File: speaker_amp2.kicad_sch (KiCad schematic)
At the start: 59 parts, among them U1 TAS5822MDCPR, U2 TAS5822MDCPR

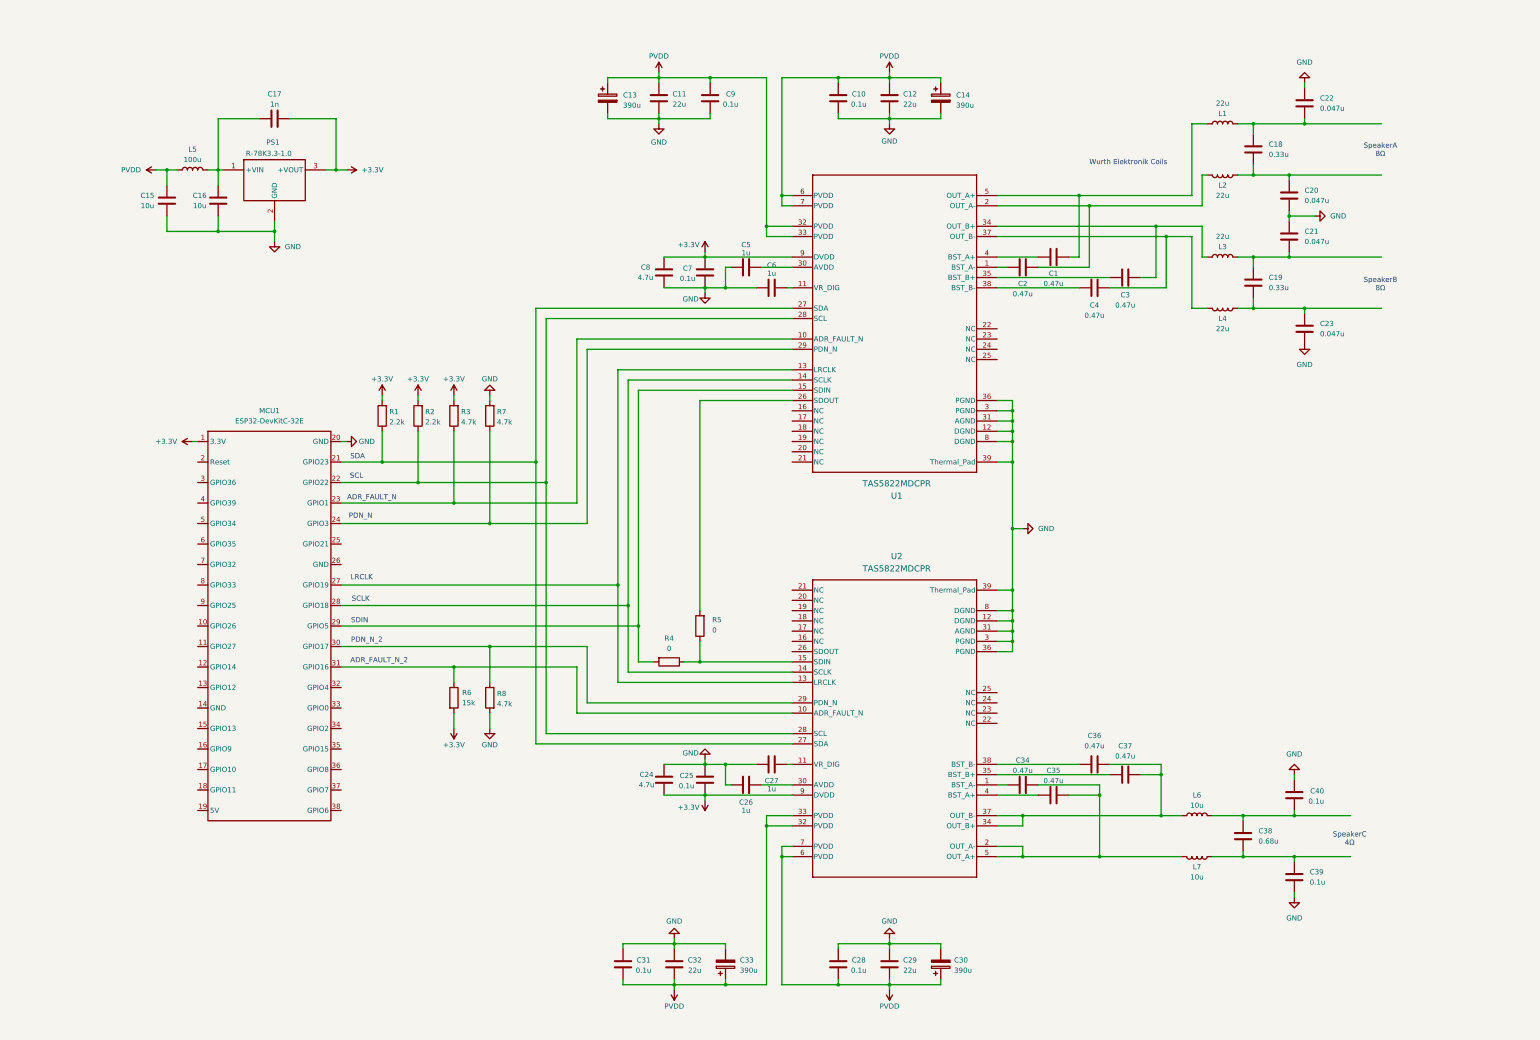
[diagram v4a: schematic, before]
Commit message: added connectors
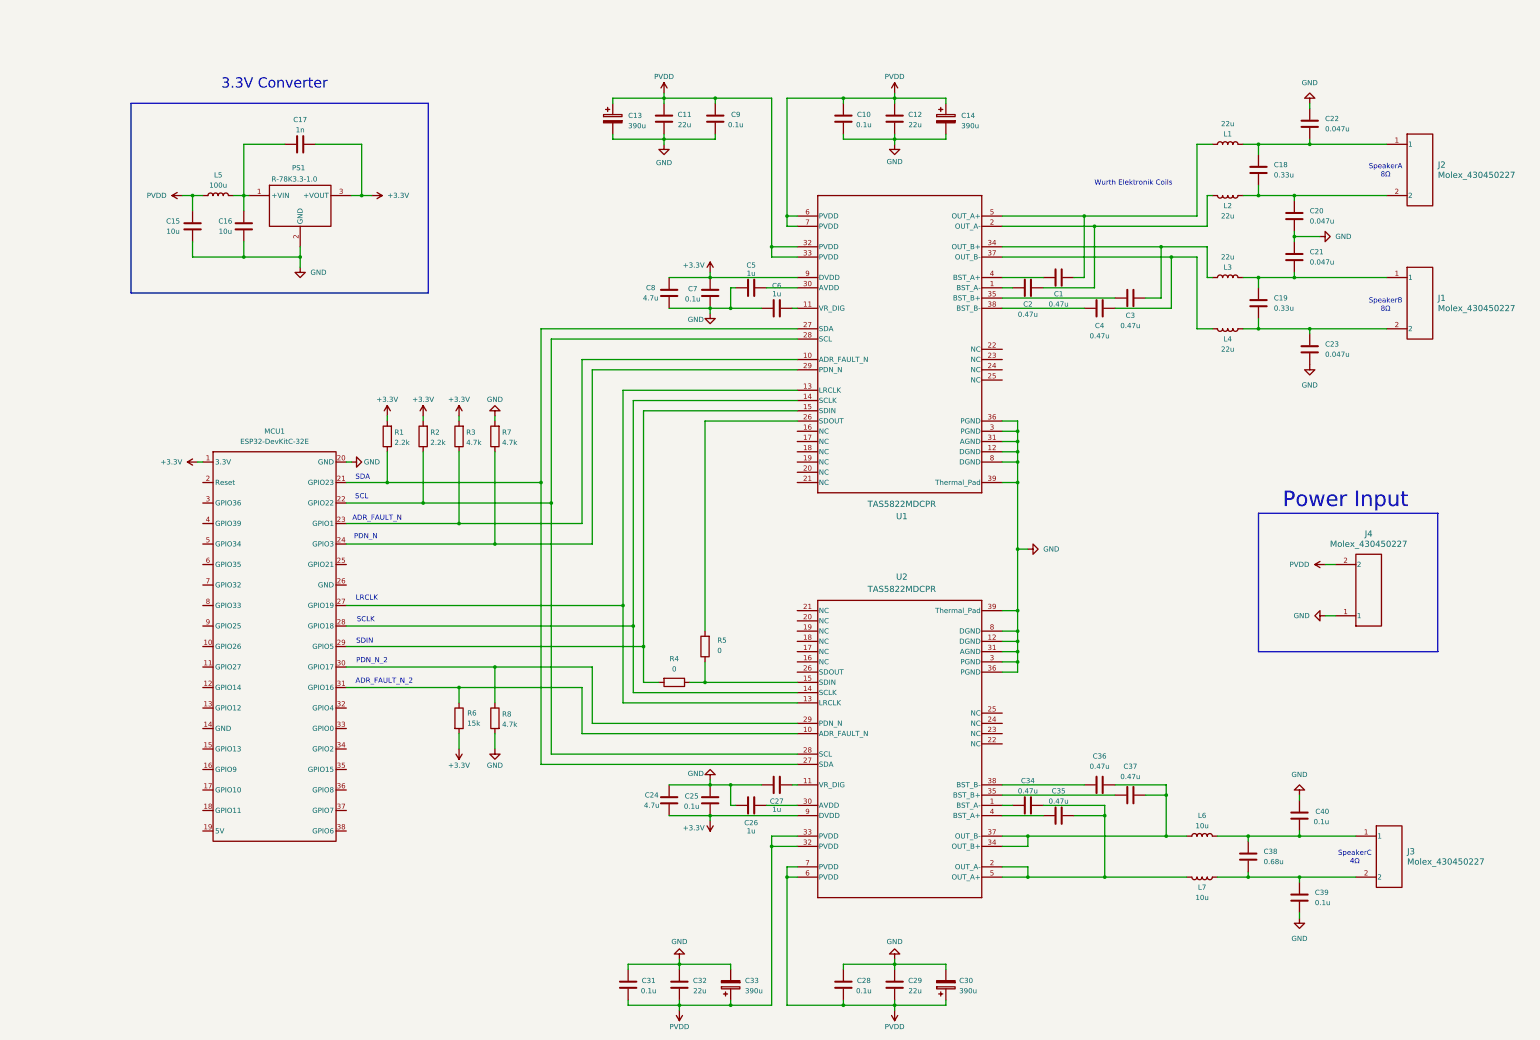
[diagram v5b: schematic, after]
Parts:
- added J1, J2, J3, J4: Molex_430450227, Speaker Amp Lib:430450227_MOLEX, symbol Speaker Amp Lib:Molex_430450227
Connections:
- net GND: now also J4.1
- net PVDD: now also J4.2
- net at C18.2, C20.1, L2.1: now also J2.2
- net at C38.1, C40.1, L6.2: now also J3.1
- net at C18.1, C22.2, L1.2: now also J2.1
- net at C19.2, C23.1, L4.1: now also J1.2
- net at C19.1, C21.2, L3.2: now also J1.1
- net at C38.2, C39.1, L7.1: now also J3.2
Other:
- note added: "3.3V Converter"
- note added: "Power Input"
- moved on the sheet: C1, C10, C11, C12, C13, C14, C15, C16, C17, C18, C19, C2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

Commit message: changes after reviewing schematic
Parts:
- added F1: 8A, Fuse:Fuse_1206_3216Metric, symbol Device:Fuse
- added R10, R9: 4.7k, Resistor_SMD:R_0805_2012Metric_Pad1.20x1.40mm_HandSolder, symbol Device:R
- C10, C25, C28, C31, C7, C9: footprint Capacitor_SMD:C_0805_2012Metric_Pad1.18x1.45mm_HandSolder -> Capacitor_SMD:C_0603_1608Metric_Pad1.08x0.95mm_HandSolder; MouserLink https://gr.mouser.com/ProductDetail/KEMET/C0805C104K5RAC741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 -> https://gr.mouser.com/ProductDetail/KEMET/C0603C104J5RACTM?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
- C11, C12, C29, C32: footprint Capacitor_SMD:C_1210_3225Metric_Pad1.33x2.70mm_HandSolder -> Capacitor_SMD:C_0805_2012Metric_Pad1.18x1.45mm_HandSolder; MouserLink https://gr.mouser.com/ProductDetail/TAIYO-YUDEN/GMK325BJ226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 -> https://gr.mouser.com/ProductDetail/TDK/C2012X5R1V226M125AC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
- C26, C27, C5, C6: footprint Capacitor_SMD:C_0805_2012Metric_Pad1.18x1.45mm_HandSolder -> Capacitor_SMD:C_0603_1608Metric_Pad1.08x0.95mm_HandSolder; MouserLink https://gr.mouser.com/ProductDetail/Samsung-Electro-Mechani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 -> https://gr.mouser.com/ProductDetail/TAIYO-YUDEN/MLAST168SB7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
- C38: footprint Capacitor_THT:C_Rect_L18.0mm_W13.0mm_P15.00mm_FKS3_FKP3 -> Speaker Amp Lib:C_Rect_L18.0mm_W13.0mm_P15.00mm_FKS3_FKP3
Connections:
- net +3.3V: now also C25.1, R10.2, R9.2; no longer C25.2
- net GND: now also C25.2, C28.2, C29.2, C31.2, C32.2; no longer C25.1, C28.1, C29.1, C31.1, C32.1
- net PVDD: now also C28.1, C29.1, C31.1, C32.1, F1.1; no longer C28.2, C29.2, C31.2, C32.2, J4.2
- net at MCU1.24 (GPIO3), R7.1, U1.29 (PDN_N): now also R9.1
- net at MCU1.30 (GPIO17), R8.1, U2.29 (PDN_N): now also R10.1
- new net: F1.2, J4.2
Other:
- note added: "I2C Address: 0x58 -> 0d88"
- note added: "I2C Address: 0x5A -> 0d90"
- moved on the sheet: C24, C8, J4, R4, R5

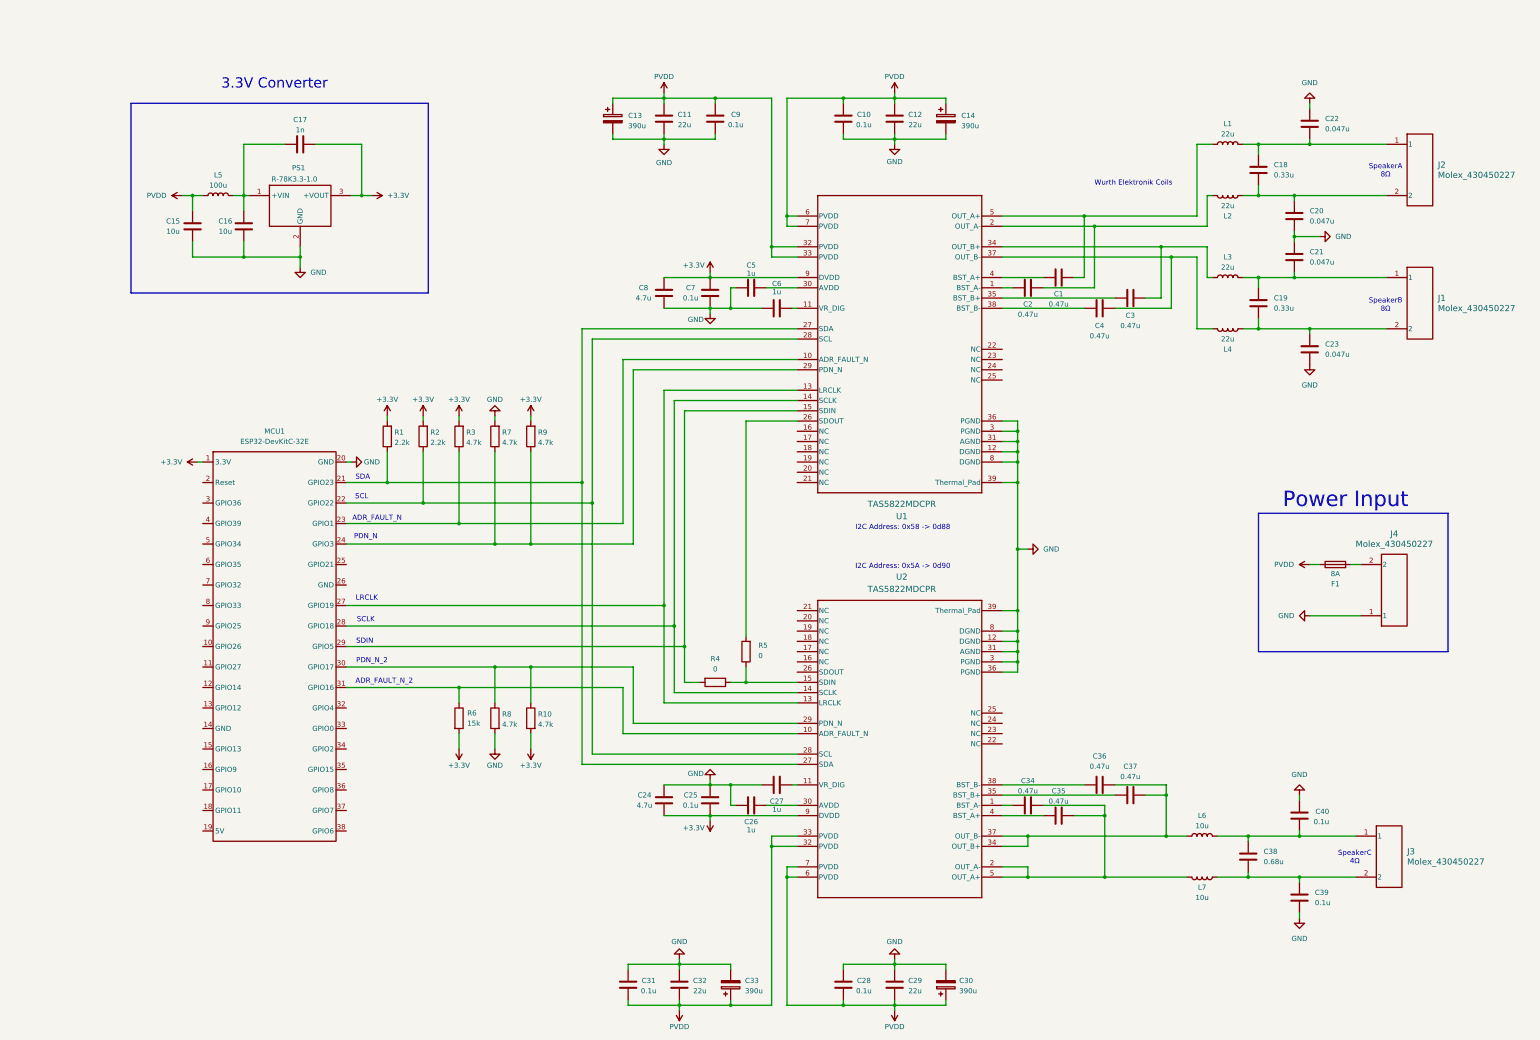
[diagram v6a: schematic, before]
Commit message: added button connector
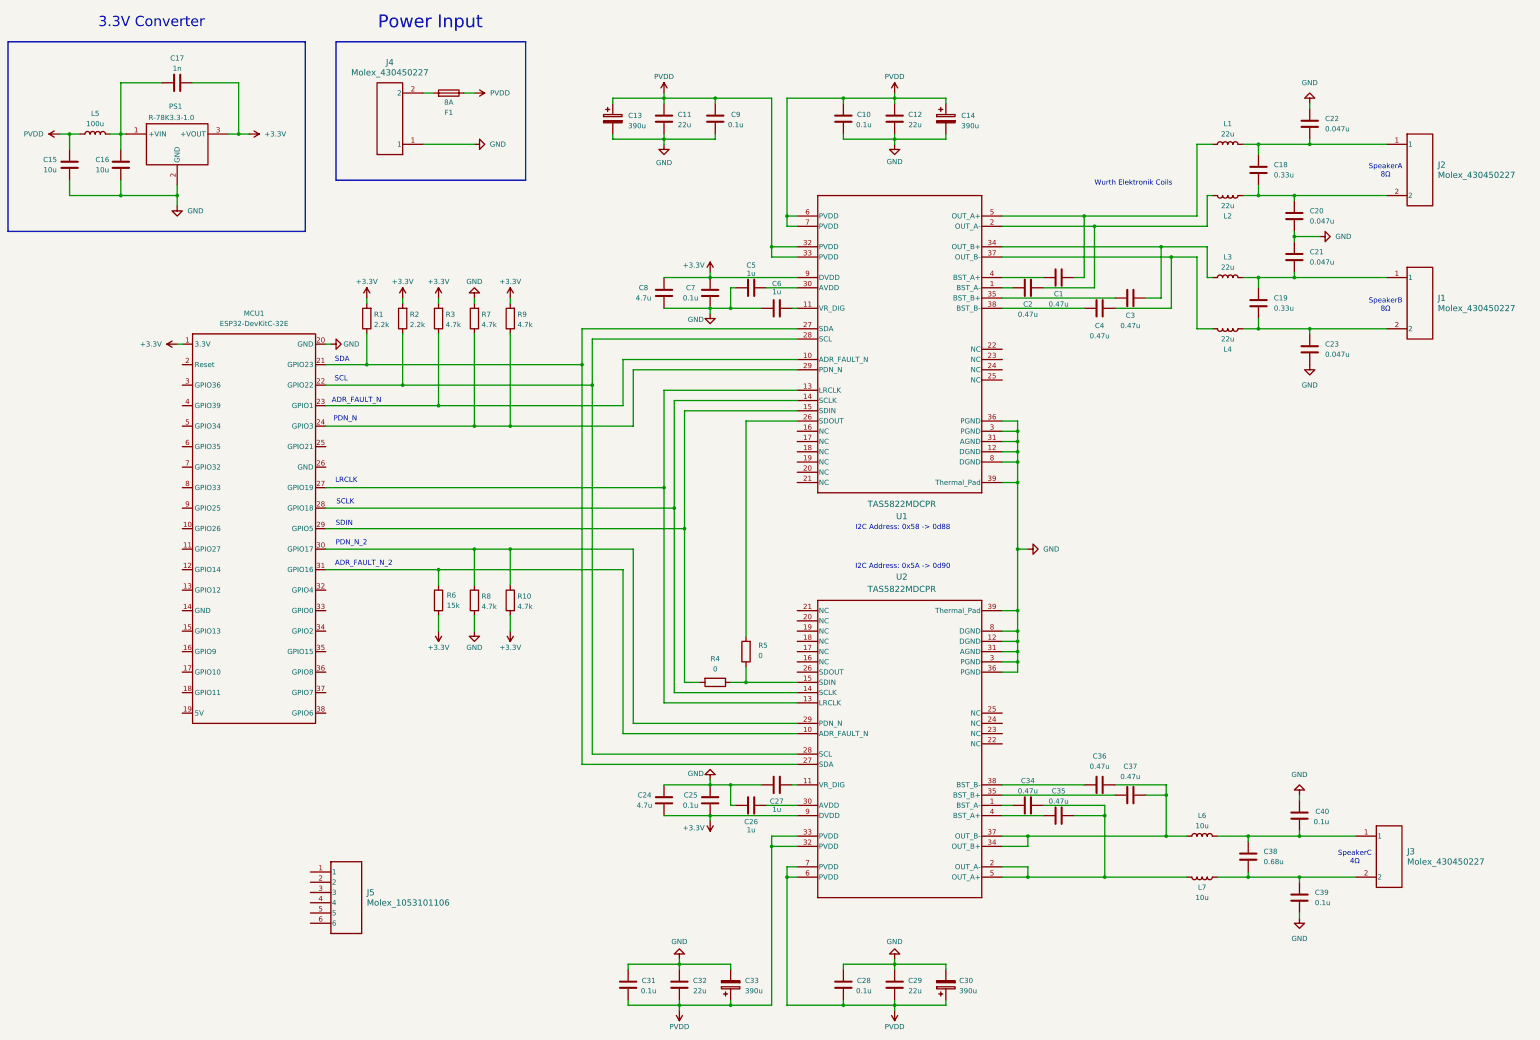
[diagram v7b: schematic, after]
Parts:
- added J5: Molex_1053101106, Speaker Amp Lib:Molex_1053101106, symbol Speaker Amp Lib:Molex_1053101106
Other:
- moved on the sheet: C15, C16, C17, F1, J4, L5, MCU1, PS1, R1, R10, R2, R3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

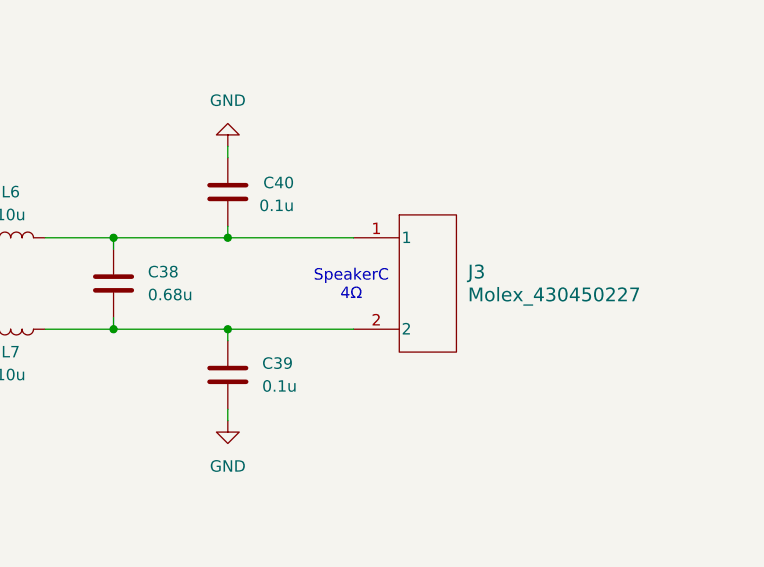
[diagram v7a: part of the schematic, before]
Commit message: fixed silkscreen on connector footprints
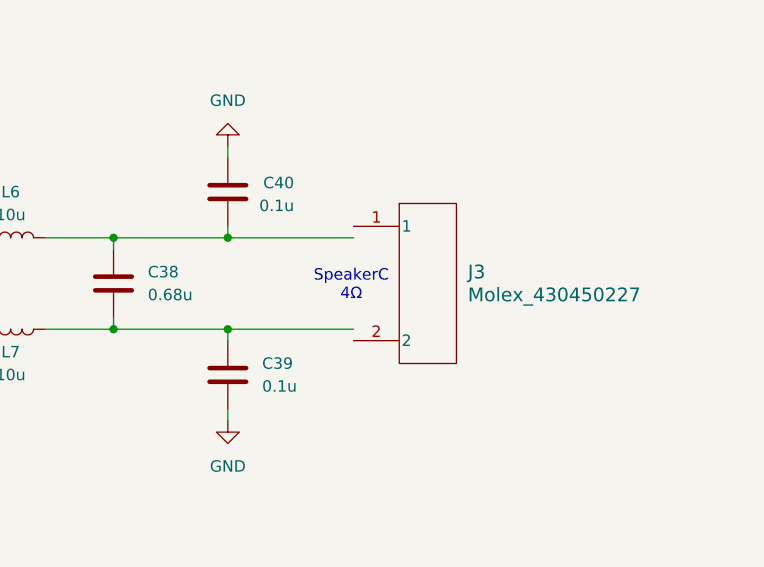
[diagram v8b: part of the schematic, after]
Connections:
- net at C38.1, C40.1, L6.2: no longer J3.1
- net at C38.2, C39.1, L7.1: no longer J3.2
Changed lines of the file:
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@@
 	)
 	(symbol
-		(lib_name "Molex_430450227_1")
 		(lib_id "Speaker Amp Lib:Molex_430450227")
 		(at 356.87 226.06 0)
@@
 	)
 	(symbol
-		(lib_name "TAS5822MDCPR_1")
 		(lib_id "Speaker Amp Lib:TAS5822MDCPR")
 		(at 218.44 68.58 0)
